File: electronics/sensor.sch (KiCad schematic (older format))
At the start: 37 parts, among them CON1 MOTOR_PWR, J1 EXP. IN, J2 EXP. OUT, P1 CONN_01X05, P10 CONN_01X04, P2 CONN_01X05, P3 CONN_01X05, P4 CONN_01X05, P5 SENSOR, P6 CONN_01X04, P7 CONN_01X04, P8 CONN_01X04, P9 SENSOR, U1 arduino_uno_shield, U10 GP2S60, U2 MIC5842, U3 74HC165, U4 MIC5842, U5 WS2812B, U6 WS2812B, U7 WS2812B, U8 WS2812B, U9 GP2S60

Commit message: Sensor schematic, starting pcb
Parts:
- removed C1, C3: 100uF, Capacitors_ThroughHole:CP_Radial_D8.0mm_P3.50mm, symbol CP1_Small
- removed C2: 0.1uF, Capacitors_ThroughHole:C_Rect_L7.0mm_W2.5mm_P5.00mm, symbol C_Small
- removed CON1: MOTOR_PWR, PJ-202A:PJ-202A, symbol BARREL_JACK
- removed D1: Mot+, LED3mmBetterSilkScreen:LED_D3.0mm, symbol Led_Small
- removed D2: 5V, LED3mmBetterSilkScreen:LED_D3.0mm, symbol Led_Small
- removed J1: EXP. IN, PinHeaders:Pin_Header_Straight_2x07_Pitch2.54mm_IDC_Shrouded, symbol CONN_02X07
- removed J2: EXP. OUT, PinHeaders:Pin_Header_Straight_2x07_Pitch2.54mm_IDC_Shrouded, symbol CONN_02X07
- removed P1, P2, P3, P4: CONN_01X05, JST_XH_Connectors:JST_XH_2-5mm_5pin, symbol CONN_01X05
- removed P10, P6, P7, P8: CONN_01X04, PinHeaders:Pin_Header_Straight_1x04, symbol CONN_01X04
- removed P9: SENSOR, PinHeaders:Pin_Header_Straight_1x03, symbol CONN_01X03
- removed R1: 2.2k, Resistors_ThroughHole:R_Axial_DIN0204_L3.6mm_D1.6mm_P7.62mm_Horizontal, symbol R_Small
- removed R2, R8: 220, Resistor0805ThroughHole:R_0805_ThroughHole, symbol R_Small
- removed R3, R4, R5, R6: 47k, Resistors_ThroughHole:R_Axial_DIN0204_L3.6mm_D1.6mm_P7.62mm_Horizontal, symbol R_Small
- removed R7: 1k, Resistors_ThroughHole:R_Axial_DIN0204_L3.6mm_D1.6mm_P7.62mm_Horizontal, symbol R_Small
- removed R9: 470, Resistors_ThroughHole:R_Axial_DIN0204_L3.6mm_D1.6mm_P7.62mm_Horizontal, symbol R_Small
- removed U1: arduino_uno_shield, ArduinoUnoShield:arduino_uno_shield, symbol arduino_uno_shield
- removed U10, U9: GP2S60, GP2S60:GP2S60_WITH_MOUNT, symbol GP2S60
- removed U2, U4: MIC5842, Housings_DIP:DIP-18_W7.62mm, symbol MIC5842
- removed U3: 74HC165, Housings_DIP:DIP-16_W7.62mm, symbol 74HC165
- removed U5, U6, U7, U8: WS2812B, LEDs:LED_WS2812B-PLCC4, symbol WS2812B
- added U1: AH1815, ah1815:AH1815, symbol AH1815
- renumbered P5 to P1
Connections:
- net labels removed: +5V, DBGLED_IN, DBGLED_OUT, GND, MOTOR_DATA_IN, MOTOR_DATA_OUT, MOTOR_LATCH, SENSE1, SENSE2, SENSE3, SENSE4, SENSOR_DATA_IN, SENSOR_DATA_OUT, SENSOR_LATCH, SPI_CLOCK, VCC
- wire segments 187 -> 8
- no-connect marks 7 -> 0
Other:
- note removed: "EXPANSION PORT"
- note removed: "Reflective IR Sensor"
- moved on the sheet: P1

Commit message: Include magnet part number with hall-effect sensor on schematic BOM; change 5V LED to use 220 ohm resistor
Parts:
- U1: DK# AH1815-P-B -> AH1815-P-B, 469-1027-ND
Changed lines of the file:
@@
 F 2 "ah1815:AH1815" H 4450 3700 60  0001 C CNN
 F 3 "" H 4450 3700 60  0001 C CNN
-F 4 "AH1815-P-B" H 4450 3700 60  0001 C CNN "DK#"
+F 4 "AH1815-P-B, 469-1027-ND" H 4450 3700 60  0001 C CNN "DK#"
 	1    4450 3700
 	1    0    0    -1

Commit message: Fix Digikey part number for AH1815 in schematic
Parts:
- U1: DK# AH1815-P-B, 469-1027-ND -> AH1815-P-BDI-ND, 469-1027-ND
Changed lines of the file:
@@
 F 2 "ah1815:AH1815" H 4450 3700 60  0001 C CNN
 F 3 "" H 4450 3700 60  0001 C CNN
-F 4 "AH1815-P-B, 469-1027-ND" H 4450 3700 60  0001 C CNN "DK#"
+F 4 "AH1815-P-BDI-ND, 469-1027-ND" H 4450 3700 60  0001 C CNN "DK#"
 	1    4450 3700
 	1    0    0    -1

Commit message: Replace AH1815 references with AH3391Q
The AH1815 hall effect sensor won't work, as it samples the magnetic field too infrequently for the precision needed, as mentioned in https://github.com/scottbez1/splitflap/issues/29#issuecomment-418163631

This replaces the AH1815 schematic/pcb module with a generic "hall_effect" module (since it seems most hall effect sensors have the same pinout and physical dimensions), and updates the schematic reference and BOM to specify AH3391Q as the preferred sensor. As noted in https://github.com/scottbez1/splitflap/issues/29#issuecomment-418234571 a number of other variants of hall effect sensor would also work, besides the AH3391Q, so the PCB silkscreen is now generic ("Hall Effect" instead of "AH1815"), with added pin labels for the hall effect sensor.
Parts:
- U1: value AH1815 -> AH3391Q; footprint ah1815:AH1815 -> hall_effect:hall_effect; symbol AH1815 -> hall_effect; DK# AH1815-P-BDI-ND, 469-1027-ND -> AH3391Q-P-BDI-ND (sensor), 469-1027-ND (magnet)
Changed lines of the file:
@@
 LIBS:MIC5842
 LIBS:ws2812b
-LIBS:ah1815
+LIBS:hall_effect
 LIBS:sensor-cache
 EELAYER 25 0
@@
 $EndComp
 $Comp
-L AH1815 U1
+L hall_effect U1
 U 1 1 5B63B9BC
 P 4450 3700
 F 0 "U1" H 4550 3900 60  0000 C CNN
-F 1 "AH1815" V 4350 3700 60  0000 C CNN
-F 2 "ah1815:AH1815" H 4450 3700 60  0001 C CNN
+F 1 "AH3391Q" V 4350 3700 60  0000 C CNN
+F 2 "hall_effect:hall_effect" H 4450 3700 60  0001 C CNN
 F 3 "" H 4450 3700 60  0001 C CNN
-F 4 "AH1815-P-BDI-ND, 469-1027-ND" H 4450 3700 60  0001 C CNN "DK#"
+F 4 "AH3391Q-P-BDI-ND (sensor), 469-1027-ND (magnet)" H 4450 3700 60  0001 C CNN "DK#"
 	1    4450 3700
 	1    0    0    -1

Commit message: Add BOM note about picking a hall effect sensor
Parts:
- U1: BOM_Note (none) -> Many hall effect sensors will work. AH3391Q is recommended,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
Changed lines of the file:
@@
 F 3 "" H 4450 3700 60  0001 C CNN
 F 4 "AH3391Q-P-BDI-ND (sensor), 469-1027-ND (magnet)" H 4450 3700 60  0001 C CNN "DK#"
+F 5 "Many hall effect sensors will work. AH3391Q is recommended, but other options that have been tested are AH3369Q, AH3366Q, AH3365Q, A1122LUA-T. If using another part, MAKE SURE it doesn't have a \"sleep\" or \"low power\" mode, as those generally sample the magnetic field too infrequently for this purpose." H 4450 3700 60  0001 C CNN "BOM_Note"
 	1    4450 3700
 	1    0    0    -1

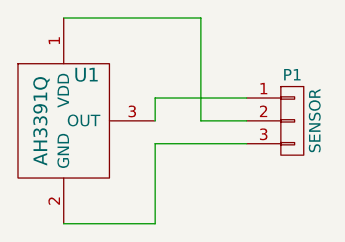
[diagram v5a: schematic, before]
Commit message: Change sensor references to U100/P100 to avoid confusion with U1/P1 on controller PCB
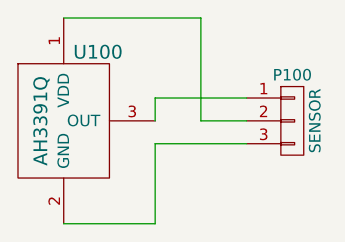
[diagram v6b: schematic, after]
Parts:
- renumbered P1 to P100, U1 to U100
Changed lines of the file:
@@
 $EndDescr
 $Comp
-L CONN_01X03 P1
+L CONN_01X03 P100
 U 1 1 56499725
 P 5450 3700
-F 0 "P1" H 5450 3900 50  0000 C CNN
+F 0 "P100" H 5450 3900 50  0000 C CNN
 F 1 "SENSOR" V 5550 3700 50  0000 C CNN
 F 2 "PinHeaders:Pin_Header_Straight_1x03" H 5450 3700 60  0001 C CNN
@@
 $EndComp
 $Comp
-L hall_effect U1
+L hall_effect U100
 U 1 1 5B63B9BC
 P 4450 3700
-F 0 "U1" H 4550 3900 60  0000 C CNN
+F 0 "U100" H 4600 4000 60  0000 C CNN
 F 1 "AH3391Q" V 4350 3700 60  0000 C CNN
 F 2 "hall_effect:hall_effect" H 4450 3700 60  0001 C CNN

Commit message: Update sensor project and fix BOM export
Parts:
- P100: symbol CONN_01X03 -> Connector_Generic:Conn_01x03
- U100: symbol hall_effect -> hall_effect:hall_effect
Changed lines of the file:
@@
-EESchema Schematic File Version 2
-LIBS:power
-LIBS:device
-LIBS:transistors
-LIBS:conn
-LIBS:linear
-LIBS:regul
-LIBS:74xx
-LIBS:cmos4000
-LIBS:adc-dac
-LIBS:memory
-LIBS:xilinx
-LIBS:microcontrollers
-LIBS:dsp
-LIBS:microchip
-LIBS:analog_switches
-LIBS:motorola
-LIBS:texas
-LIBS:intel
-LIBS:audio
-LIBS:interface
-LIBS:digital-audio
-LIBS:philips
-LIBS:display
-LIBS:cypress
-LIBS:siliconi
-LIBS:opto
-LIBS:atmel
-LIBS:contrib
-LIBS:valves
-LIBS:gp2s60
-LIBS:mount
-LIBS:arduino_uno_shield
-LIBS:74HC165
-LIBS:MIC5842
-LIBS:ws2812b
-LIBS:hall_effect
+EESchema Schematic File Version 4
 LIBS:sensor-cache
-EELAYER 25 0
+EELAYER 26 0
 EELAYER END
 $Descr A4 11693 8268
@@
 $EndDescr
 $Comp
-L CONN_01X03 P100
+L Connector_Generic:Conn_01x03 P100
 U 1 1 56499725
 P 5450 3700
@@
 $EndComp
 $Comp
-L hall_effect U100
+L hall_effect:hall_effect U100
 U 1 1 5B63B9BC
 P 4450 3700
@@
 	4850 3600 4850 3700
 Wire Wire Line
-	5250 3700 5050 3700
-Wire Wire Line
 	5050 3700 5050 3250
 Wire Wire Line
@@
 Wire Wire Line
 	4850 3800 5250 3800
+Wire Wire Line
+	5050 3700 5250 3700
 $EndSCHEMATC
